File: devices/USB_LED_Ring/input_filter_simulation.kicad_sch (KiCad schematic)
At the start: 19 parts

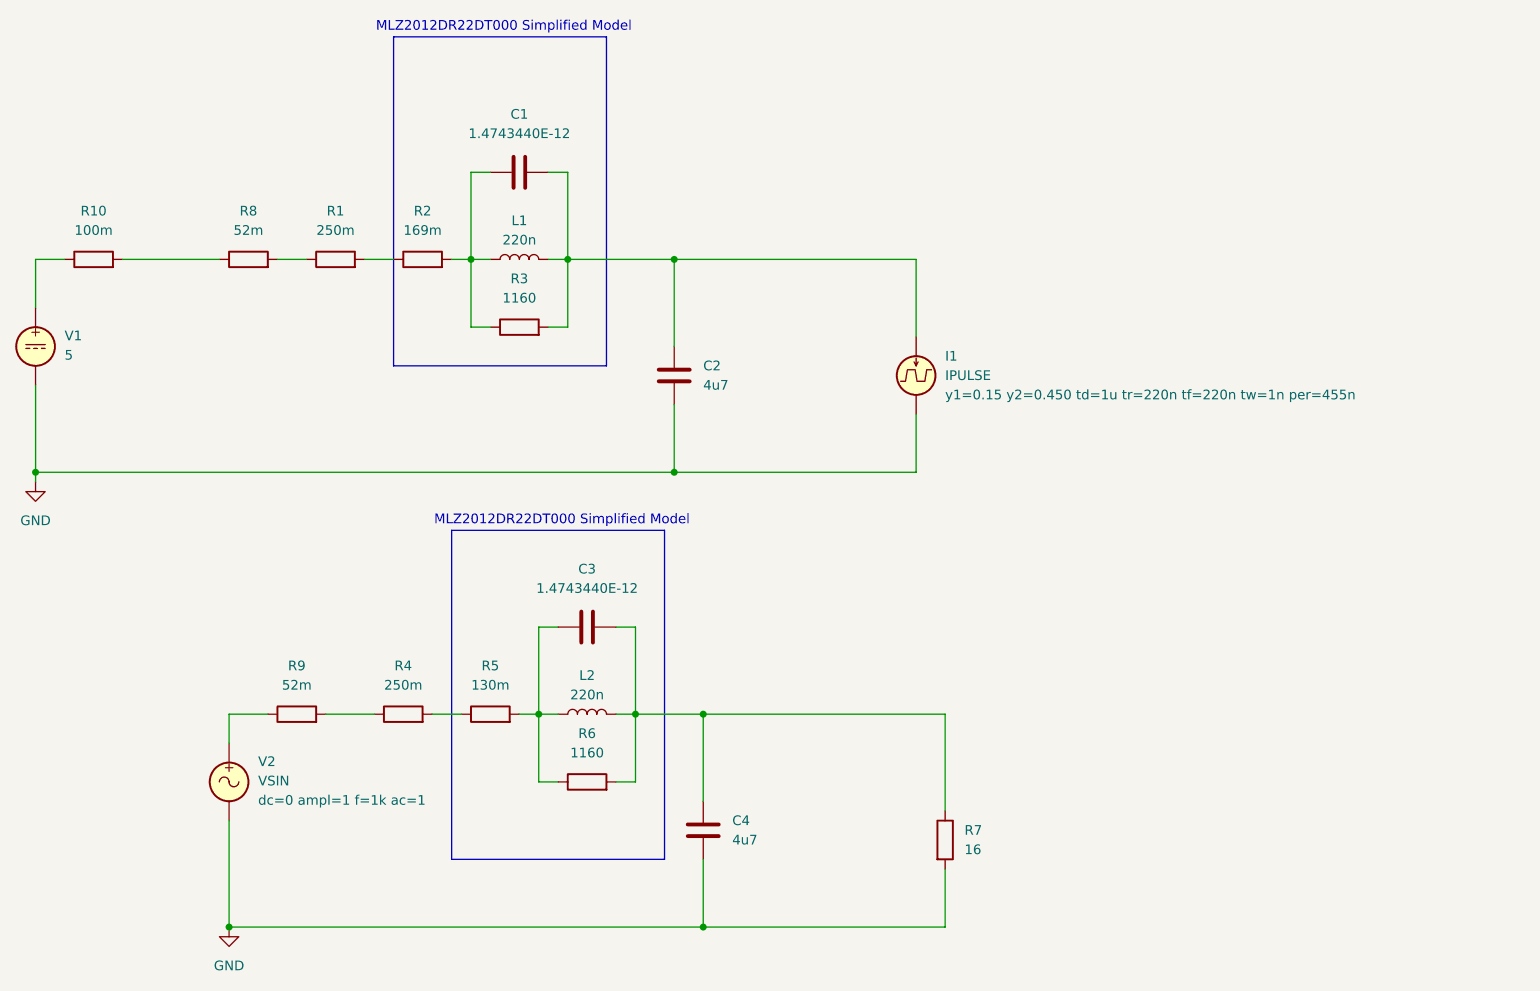
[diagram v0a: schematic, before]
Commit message: Improves input filter for LED driver
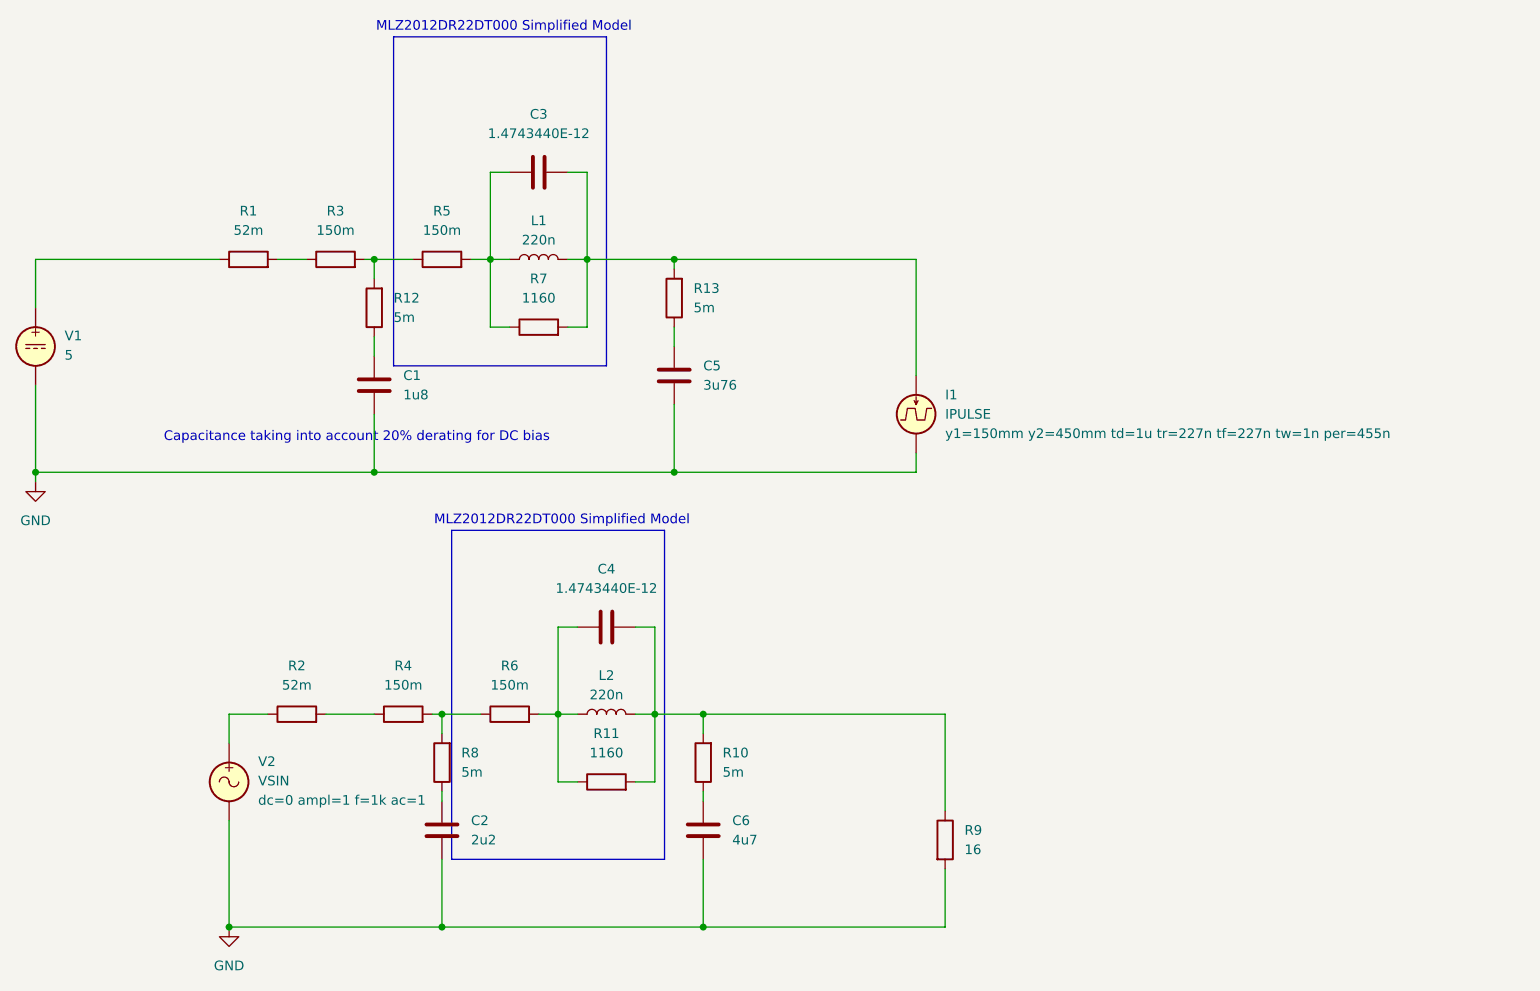
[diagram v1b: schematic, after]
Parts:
- removed C3: 1.4743440E-12, symbol Device:C
- removed R5: 130m, symbol Device:R
- added C1: 1u8, symbol Device:C
- added C2: 2u2, symbol Device:C
- added C4: 1.4743440E-12, symbol Device:C
- added R11: 1160, symbol Device:R
- added R12, R13, R8: 5m, symbol Device:R
- C5: renamed from C2; value 4u7 -> 3u76
- R10: value 100m -> 5m
- R3: renamed from R1; value 250m -> 150m
- R4: value 250m -> 150m
- R5: renamed from R2; value 169m -> 150m
- R6: value 1160 -> 150m
- renumbered C1 to C3, C4 to C6, R8 to R1, R9 to R2, R3 to R7, R7 to R9
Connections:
- net GND: now also C1.2, C2.2
- net at C3.2, I1.1, L1.2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: now also R13.2; no longer C5.1
- net at L2.2, R9.1: now also R10.2, C4.2, R11.2; no longer C6.1, R6.2
- net at R4.2: now also R6.1, R8.2
- net at R3.2, R5.1: now also R12.2
- net at R10.1: now also C6.1; no longer V1.1
- net at R1.1: now also V1.1; no longer R10.2
- net at L2.1: now also R6.2, C4.1, R11.1; no longer R6.1
- new net: C2.1, R8.1
- new net: C5.1, R13.1
- new net: C1.1, R12.1
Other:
- note added: "Capacitance taking into account 20% derating for DC bias"
- moved on the sheet: C3, I1, L1, R5, R7

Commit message: !fixup
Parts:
- removed C1: 1u8, symbol Device:C
- removed C3, C4: 1.4743440E-12, symbol Device:C
- removed C5: 3u76, symbol Device:C
- removed R1: 52m, symbol Device:R
- removed R10, R12, R13, R8: 5m, symbol Device:R
- removed R11, R7: 1160, symbol Device:R
- removed R5, R6: 150m, symbol Device:R
- removed R9: 16, symbol Device:R
- removed V1: 5, symbol Simulation_SPICE:VDC
- removed V2: VSIN, symbol Simulation_SPICE:VSIN
- added V1: VPULSE, symbol Simulation_SPICE:VPULSE
- C2: value 2u2 -> 4u7
- L1: value 220n -> 1u
- L2: value 220n -> ${SIM.PARAMS}
- R2: value 52m -> 100m
- R3: value 150m -> 28m
- R4: value 150m -> 100m
- renumbered C6 to C1
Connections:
- net GND: now also V1.2
- net at L1.1: now also R4.1
- net VIN: now reaches L1.2
- net VIN: now also R3.2; no longer I1.1
- net at R4.2: now also V1.1
- net at L2.1: now also C2.1, R2.1
- net VOUT: now reaches L2.2
- net VOUT: now also C1.1, I1.1
- net at R2.2: now also R3.1; no longer R4.1
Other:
- note removed: "Capacitance taking into account 20% derating for DC bias"
- note removed: "MLZ2012DR22DT000 Simplified Model"
- moved on the sheet: C1
